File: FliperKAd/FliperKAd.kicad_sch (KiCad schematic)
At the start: 5 parts, among them Q1 NMOS

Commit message: Avancement du PCB
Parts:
- added C10, C9: 100 nF, Capacitor_SMD:C_0402_1005Metric, symbol Device:C_Small
- added C11: 100nF, Capacitor_SMD:C_0603_1608Metric, symbol Device:C_Small
- added C6: 1 µF, Capacitor_SMD:C_0603_1608Metric, symbol Device:C_Small
- added C7: 4.7 µF, Capacitor_SMD:C_0603_1608Metric, symbol Device:C_Small
- added C8: 10 nF, Capacitor_SMD:C_0402_1005Metric, symbol Device:C_Small
- added D2: Green_LED, LED_SMD:LED_0603_1608Metric, symbol Device:LED
- added H1, H2, H3, H4: MountingHole_Pad, MountingHole:MountingHole_3.2mm_M3_Pad_Via, symbol Mechanical:MountingHole_Pad
- added J4: Conn_ST_STDC14, Connector_PinHeader_1.27mm:PinHeader_2x07_P1.27mm_Vertical_SMD, symbol Connector:Conn_ST_STDC14
- added J5: Conn_01x02, Connector_JST:JST_XH_B2B-XH-A_1x02_P2.50mm_Vertical, symbol Connector_Generic:Conn_01x02
- added L2: 39 nH, Inductor_SMD:L_0603_1608Metric, symbol Device:L_Small
- added R2: 1k, Resistor_SMD:R_0603_1608Metric, symbol Device:R_Small
- added U1: STM32G431KBTx, Package_QFP:LQFP-32_7x7mm_P0.8mm, symbol MCU_ST_STM32G4:STM32G431KBTx
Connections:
- net 24V is gone; now on an unnamed net: Q1.3 (S)
- net CommandeBuck: now also U1.9 (PA4)
- net GND: now also C10.2, C11.2, C6.2, C7.2, C8.2, C9.2, H1.1, H2.1, H3.1, H4.1, J4.11 (GNDDetect), J4.5 (GND), J4.7 (GND), J5.2 (Pin_2), R2.2, U1.14 (VSSA), U1.16 (VSS), U1.32 (VSS)
- net at D1.1 (K), L1.1: no longer Q1.1 (D)
- net 3.3V renamed +3.3V
- net +3.3V: now also C10.1, C7.1, C9.1, J4.3 (VCC), L2.2, U1.1 (VDD), U1.17 (VDD)
- new net +24V: J5.1 (Pin_1), Q1.1 (D)
- new net +3.3VA: C6.1, C8.1, L2.1, U1.15 (VDDA)
- new net CommandeSolénoîde: U1.10 (PA5)
- new net LED_Stat: D2.1 (K), R2.1
- new net LED_Status: D2.2 (A), U1.18 (PA8)
- new net NRST: C11.1, J4.12 (~{RST}), U1.4 (PG10)
- new net SYS_SWCLK: J4.6 (JCLK/SWCLK), U1.24 (PA14)
- new net SYS_SWDIO: J4.4 (JTMS/SWDIO), U1.23 (PA13)
- new net USART2_RX: J4.13 (VCP_RX), U1.8 (PA3)
- new net USART2_TX: J4.14 (VCP_TX), U1.7 (PA2)
- no-connect marks 0 -> 15
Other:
- company: (none) -> ENSEA
- title: (none) -> PCB_Solénoide
- moved on the sheet: Q1

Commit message: Fin de séance du 30
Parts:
- added C2: 10 µ, symbol Device:C_Small
- added C3: 1 µ, symbol Device:C_Small
- added C4: 47 µ, symbol Device:C_Small
- added R3: 137k, symbol Device:R_Small
- added R4: 402k, symbol Device:R_Small
- added R5: R_Small, symbol Device:R_Small
- added U2, U3: MCP1640x-xMC, Package_DFN_QFN:DFN-8-1EP_3x2mm_P0.5mm_EP1.75x1.45mm, symbol Lib:MCP1640x-xMC
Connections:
- net +24V: now also C2.1, U2.4 (Vin), U2.5 (Vin)
- net +3.3V: now also C4.1, R4.1, U2.6 (Vout), U2.7 (Vout)
- net GND: now also C2.2, C3.2, C4.2, R3.2, R5.2, U2.10 (AGND), U2.13 (PGND)
- new net: C3.1, U2.1 (FSW)
- new net: R3.1, R4.2, U2.2 (FB)
- new net: R5.1, U2.3 (VCC)
- new net: U2.12 (EN), U2.9 (Vin)
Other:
- note added: "WPME"

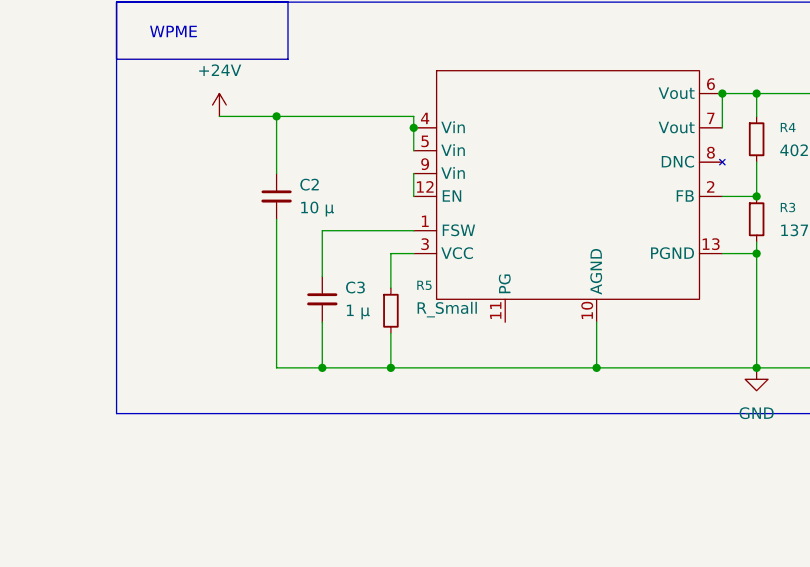
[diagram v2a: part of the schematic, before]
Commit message: Ajout du dossier Doc
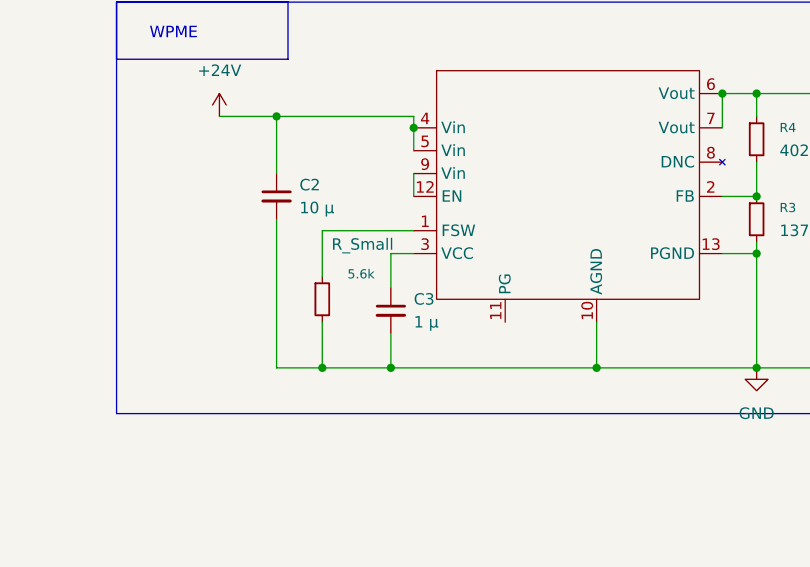
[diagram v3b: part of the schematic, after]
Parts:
- renumbered R5 to 5.6k
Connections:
- net at C3.1: now also U2.3 (VCC); no longer U2.1 (FSW)
- net at 5.6k.1: now also U2.1 (FSW); no longer U2.3 (VCC)
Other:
- moved on the sheet: 5.6k, C3
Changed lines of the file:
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@@
 	)
 	(junction
-		(at 208.28 160.02)
-		(diameter 0)
-		(color 0 0 0 0)
-	)
-	(junction
 		(at 248.92 160.02)
 		(diameter 0)
@@
 	)
 	(junction
-		(at 200.66 160.02)
-		(diameter 0)
-		(color 0 0 0 0)
-	)
-	(junction
 		(at 57.15 173.99)
 		(diameter 0)
@@
 	)
 	(junction
+		(at 208.28 160.02)
+		(diameter 0)
+		(color 0 0 0 0)
+	)
+	(junction
 		(at 243.84 74.93)
 		(diameter 0)
@@
 	)
 	(junction
+		(at 200.66 160.02)
+		(diameter 0)
+		(color 0 0 0 0)
+	)
+	(junction
 		(at 250.19 33.02)
 		(diameter 0)
@@
 	(wire
 		(pts
-			(xy 208.28 147.32) (xy 208.28 151.13)
-		)
-		(stroke
-			(width 0)
-			(type default)
-		)
-	)
-	(wire
-		(pts
 			(xy 243.84 87.63) (xy 261.62 87.63)
 		)
@@
 	(wire
 		(pts
-			(xy 200.66 154.94) (xy 200.66 160.02)
+			(xy 200.66 144.78) (xy 200.66 149.86)
 		)
 		(stroke
@@
 	(wire
 		(pts
-			(xy 200.66 144.78) (xy 200.66 149.86)
+			(xy 200.66 154.94) (xy 200.66 160.02)
 		)
 		(stroke
@@
 	(wire
 		(pts
-			(xy 208.28 156.21) (xy 208.28 160.02)
+			(xy 60.96 88.9) (xy 60.96 91.44)
 		)
 		(stroke
@@
 	(wire
 		(pts
-			(xy 60.96 88.9) (xy 60.96 91.44)
+			(xy 208.28 160.02) (xy 231.14 160.02)
 		)
 		(stroke
@@
 	(wire
 		(pts
+			(xy 208.28 147.32) (xy 208.28 151.13)
+		)
+		(stroke
+			(width 0)
+			(type default)
+		)
+	)
+	(wire
+		(pts
 			(xy 210.82 132.08) (xy 210.82 133.35)
 		)
@@
 	(wire
 		(pts
+			(xy 208.28 156.21) (xy 208.28 160.02)
+		)
+		(stroke
+			(width 0)
+			(type default)
+		)
+	)
+	(wire
+		(pts
 			(xy 261.62 87.63) (xy 261.62 82.55)
 		)
@@
 	(wire
 		(pts
-			(xy 200.66 160.02) (xy 208.28 160.02)
+			(xy 226.06 74.93) (xy 231.14 74.93)
 		)
 		(stroke
@@
 	(wire
 		(pts
-			(xy 226.06 74.93) (xy 231.14 74.93)
+			(xy 200.66 160.02) (xy 208.28 160.02)
 		)
 		(stroke
@@
 	(wire
 		(pts
-			(xy 208.28 160.02) (xy 231.14 160.02)
+			(xy 195.58 160.02) (xy 200.66 160.02)
 		)
 		(stroke
@@
 	(wire
 		(pts
-			(xy 195.58 160.02) (xy 200.66 160.02)
-		)
-		(stroke
-			(width 0)
-			(type default)
-		)
-	)
-	(wire
-		(pts
 			(xy 240.03 60.96) (xy 236.22 60.96)
 		)
@@
 	(symbol
 		(lib_id "Device:C_Small")
-		(at 200.66 152.4 0)
+		(at 208.28 153.67 0)
 		(unit 1)
 		(exclude_from_sim no)
@@
 		(fields_autoplaced yes)
 		(property "Reference" "C3"
-			(at 203.2 151.1362 0)
+			(at 210.82 152.4062 0)
 			(effects
 				(font
@@
 		)
 		(property "Value" "1 µ"
-			(at 203.2 153.6762 0)
+			(at 210.82 154.9462 0)
 			(effects
 				(font
@@
 		)
 		(property "Footprint" ""
-			(at 200.66 152.4 0)
+			(at 208.28 153.67 0)
 			(effects
 				(font
@@
 		)
 		(property "Datasheet" "~"
-			(at 200.66 152.4 0)
+			(at 208.28 153.67 0)
 			(effects
 				(font
@@
 		)
 		(property "Description" "Unpolarized capacitor, small symbol"
-			(at 200.66 152.4 0)
+			(at 208.28 153.67 0)
 			(effects
 				(font
@@
 		(lib_name "R_Small_1")
 		(lib_id "Device:R_Small")
-		(at 208.28 153.67 0)
+		(at 200.66 152.4 0)
 		(unit 1)
 		(exclude_from_sim no)
@@
 		(on_board yes)
 		(dnp no)
-		(property "Reference" "R5"
-			(at 211.074 150.876 0)
+		(property "Reference" "5.6k"
+			(at 203.454 149.606 0)
 			(effects
 				(font
@@
 		)
 		(property "Value" "R_Small"
-			(at 211.074 153.416 0)
+			(at 201.676 146.304 0)
 			(effects
 				(font
@@
 		)
 		(property "Footprint" ""
-			(at 208.28 153.67 0)
+			(at 200.66 152.4 0)
 			(effects
 				(font
@@
 		)
 		(property "Datasheet" "~"
-			(at 208.28 153.67 0)
+			(at 200.66 152.4 0)
 			(effects
 				(font
@@
 		)
 		(property "Description" "Resistor, small symbol"
-			(at 208.28 153.67 0)
+			(at 200.66 152.4 0)
 			(effects
 				(font
@@
 			(project "FliperKAd"
 				(path "/27859523-150b-47ee-b996-34d2328aaeb5"
-					(reference "R5")
+					(reference "5.6k")
 					(unit 1)
 				)

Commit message: Finalisation schematics + empreintes
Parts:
- removed C1: C_Small, symbol Device:C_Small
- removed D1: D_Small, symbol Device:D_Small
- removed D2: Green_LED, LED_SMD:LED_0603_1608Metric, symbol Device:LED
- removed J4: Conn_ST_STDC14, Connector_PinHeader_1.27mm:PinHeader_2x07_P1.27mm_Vertical_SMD, symbol Connector:Conn_ST_STDC14
- removed L1: L_Small, symbol Device:L_Small
- removed Q1: NMOS, symbol Simulation_SPICE:NMOS
- removed R2: 1k, Resistor_SMD:R_0603_1608Metric, symbol Device:R_Small
- removed U2: MCP1640x-xMC, Package_DFN_QFN:DFN-8-1EP_3x2mm_P0.5mm_EP1.75x1.45mm, symbol Lib:MCP1640x-xMC
- added D1: LED_Small, LED_SMD:LED_0603_1608Metric, symbol Device:LED_Small
- added J1: Conn_01x02, Connector_JST:JST_XH_B2B-XH-A_1x02_P2.50mm_Vertical, symbol Connector_Generic:Conn_01x02
- added J2: Conn_ST_STDC14, Connector_PinHeader_1.27mm:PinHeader_2x07_P1.27mm_Vertical_SMD, symbol Connector:Conn_ST_STDC14
- added TP1: 24V, TestPoint:TestPoint_Pad_D2.0mm, symbol Connector:TestPoint
- added TP2: 3.3V, TestPoint:TestPoint_Pad_D2.0mm, symbol Connector:TestPoint
- C2, C3, C4: footprint (none) -> Capacitor_SMD:C_0603_1608Metric
- R1: value R_Small -> 1k; footprint (none) -> Resistor_SMD:R_0603_1608Metric
- R3, R4: footprint (none) -> Resistor_SMD:R_0603_1608Metric
- R5: renamed from 5.6k; value R_Small -> 5.6k; footprint (none) -> Resistor_SMD:R_0603_1608Metric
- U3: footprint Package_DFN_QFN:DFN-8-1EP_3x2mm_P0.5mm_EP1.75x1.45mm -> Perso:WPME_Magic
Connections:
- net +24V: now also U3.4 (Vin), U3.5 (Vin), TP1.1
- net +3.3V: now also U3.6 (Vout), U3.7 (Vout), J2.3 (VCC), TP2.1; no longer R1.1
- net GND: now also U3.10 (AGND), U3.13 (PGND), J1.2 (Pin_2), J2.11 (GNDDetect), J2.5 (GND), J2.7 (GND)
- net LED_Stat: now also R1.1, D1.1 (K)
- net LED_Status: now also D1.2 (A)
- net NRST: now also J2.12 (~{RST})
- net SYS_SWCLK: now also J2.6 (JCLK/SWCLK)
- net SYS_SWDIO: now also J2.4 (JTMS/SWDIO)
- net USART2_RX: now also J2.13 (VCP_RX)
- net USART2_TX: now also J2.14 (VCP_TX)
- net at C3.1: now also U3.3 (VCC)
- net at R3.1, R4.2: now also U3.2 (FB)
- net Bouton_Actif: now reaches U1.19 (PA9)
- net Bouton_Actif: now also J1.1 (Pin_1)
- net at U3.1 (FSW): now also R5.1
- net at U3.12 (EN): now also U3.9 (Vin)
- net CommandeBuck: no longer names the net of U1.9 (PA4)
- net CommandeSolénoîde: no longer names the net of U1.10 (PA5)
- no-connect marks 15 -> 23
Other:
- note added: "Programmer"
- note removed: "Buck"
- moved on the sheet: J5

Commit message: PCB Routé
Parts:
- added JP1: SolderJumper_2_Open, Jumper:SolderJumper-2_P1.3mm_Open_TrianglePad1.0x1.5mm, symbol Jumper:SolderJumper_2_Open
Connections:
- net +3.3V: now also JP1.2 (B); no longer C4.1, R4.1, TP2.1, U3.6 (Vout), U3.7 (Vout)
- new net Test 3.3: C4.1, JP1.1 (A), R4.1, TP2.1, U3.6 (Vout), U3.7 (Vout)
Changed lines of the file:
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@@
 	(wire
 		(pts
-			(xy 269.24 129.54) (xy 274.32 129.54)
+			(xy 269.24 129.54) (xy 273.05 129.54)
 		)
 		(stroke
@@
 	(wire
 		(pts
-			(xy 95.25 66.04) (xy 73.66 66.04)
+			(xy 77.47 66.04) (xy 73.66 66.04)
 		)
 		(stroke
@@
 	(wire
 		(pts
+			(xy 78.74 63.5) (xy 73.66 63.5)
+		)
+		(stroke
+			(width 0)
+			(type default)
+		)
+	)
+	(wire
+		(pts
 			(xy 60.96 88.9) (xy 60.96 91.44)
 		)
@@
 	(wire
 		(pts
+			(xy 280.67 127) (xy 280.67 129.54)
+		)
+		(stroke
+			(width 0)
+			(type default)
+		)
+	)
+	(wire
+		(pts
 			(xy 195.58 132.08) (xy 203.2 132.08)
 		)
@@
 		)
 	)
+	(label "Test 3.3"
+		(at 252.73 129.54 0)
+		(effects
+			(font
+				(size 1.27 1.27)
+			)
+			(justify left bottom)
+		)
+	)
 	(label "LED_Stat"
 		(at 21.59 100.33 0)
@@
 	(global_label "Bouton_Actif"
 		(shape input)
-		(at 95.25 66.04 0)
+		(at 77.47 66.04 0)
 		(fields_autoplaced yes)
 		(effects
@@
 		)
 		(property "Intersheetrefs" "${INTERSHEET_REFS}"
-			(at 110.0279 66.04 0)
+			(at 92.2479 66.04 0)
 			(effects
 				(font
@@
 	(global_label "LED_Status"
 		(shape input)
-		(at 73.66 63.5 0)
+		(at 78.74 63.5 0)
 		(fields_autoplaced yes)
 		(effects
@@
 		)
 		(property "Intersheetrefs" "${INTERSHEET_REFS}"
-			(at 87.0469 63.5 0)
+			(at 92.1269 63.5 0)
 			(effects
 				(font
@@
 	)
 	(symbol
+		(lib_id "Jumper:SolderJumper_2_Open")
+		(at 276.86 129.54 0)
+		(unit 1)
+		(exclude_from_sim no)
+		(in_bom no)
+		(on_board yes)
+		(dnp no)
+		(fields_autoplaced yes)
+		(property "Reference" "JP1"
+			(at 276.86 123.19 0)
+			(effects
+				(font
+					(size 1.27 1.27)
+				)
+			)
+		)
+		(property "Value" "SolderJumper_2_Open"
+			(at 276.86 125.73 0)
+			(effects
+				(font
+					(size 1.27 1.27)
+				)
+			)
+		)
+		(property "Footprint" "Jumper:SolderJumper-2_P1.3mm_Open_TrianglePad1.0x1.5mm"
+			(at 276.86 129.54 0)
+			(effects
+				(font
+					(size 1.27 1.27)
+				)
+				(hide yes)
+			)
+		)
+		(property "Datasheet" "~"
+			(at 276.86 129.54 0)
+			(effects
+				(font
+					(size 1.27 1.27)
+				)
+				(hide yes)
+			)
+		)
+		(property "Description" "Solder Jumper, 2-pole, open"
+			(at 276.86 129.54 0)
+			(effects
+				(font
+					(size 1.27 1.27)
+				)
+				(hide yes)
+			)
+		)
+		(pin "2"
+		)
+		(pin "1"
+		)
+		(instances
+			(project ""
+				(path "/27859523-150b-47ee-b996-34d2328aaeb5"
+					(reference "JP1")
+					(unit 1)
+				)
+			)
+		)
+	)
+	(symbol
 		(lib_id "Mechanical:MountingHole_Pad")
 		(at 259.08 20.32 270)
@@
 	(symbol
 		(lib_id "power:+3.3V")
-		(at 274.32 129.54 0)
+		(at 280.67 127 0)
 		(unit 1)
 		(exclude_from_sim no)
@@
 		(fields_autoplaced yes)
 		(property "Reference" "#PWR017"
-			(at 274.32 133.35 0)
+			(at 280.67 130.81 0)
 			(effects
 				(font
@@
 		)
 		(property "Value" "+3.3V"
-			(at 274.32 124.46 0)
+			(at 280.67 121.92 0)
 			(effects
 				(font
@@
 		)
 		(property "Footprint" ""
-			(at 274.32 129.54 0)
+			(at 280.67 127 0)
 			(effects
 				(font
@@
 		)
 		(property "Datasheet" ""
-			(at 274.32 129.54 0)
+			(at 280.67 127 0)
 			(effects
 				(font
@@
 		)
 		(property "Description" "Power symbol creates a global label with name \"+3.3V\""
-			(at 274.32 129.54 0)
+			(at 280.67 127 0)
 			(effects
 				(font

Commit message: Manque un truc
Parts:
- added J3: Conn_01x02, Connector_JST:JST_XH_B2B-XH-A_1x02_P2.50mm_Vertical, symbol Connector_Generic:Conn_01x02
- added Q1: NMOS, symbol Simulation_SPICE:NMOS
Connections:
- net GND: now also J3.2 (Pin_2)
- net Com-Sol: now reaches U1.20 (PA10)
- net Com-Sol: now also Q1.2 (G)
- new net Sortie-Solénoide: J3.1 (Pin_1)
- no-connect marks 23 -> 22

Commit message: just in time
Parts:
- added D2, D3: 1N4148WS, Diode_SMD:D_SOD-323, symbol Diode:1N4148WS
- added J4: Conn_01x02, Connector_JST:JST_XH_B2B-XH-A_1x02_P2.50mm_Vertical, symbol Connector_Generic:Conn_01x02
- added Q2: NMOS, Package_TO_SOT_SMD:TO-263-3_TabPin4, symbol Simulation_SPICE:NMOS
- added R10, R11: 4.7, Resistor_SMD:R_0603_1608Metric, symbol Device:R_Small
- added R12, R2, R6, R7, R8, R9: 10k, Resistor_SMD:R_0603_1608Metric, symbol Device:R_Small
- added U4: ~, Perso:MIC4426, symbol Lib:MIC4426
- Q1: footprint (none) -> Package_TO_SOT_SMD:TO-263-3_TabPin4
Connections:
- net Sortie-Solénoide is gone; now on net +24V: J3.1 (Pin_1)
- net +24V: now also D2.1 (K), D3.1 (K), J4.1 (Pin_1), R6.1
- net GND: now also Q1.3 (S), Q2.3 (S), R12.2, R2.2, R7.2, R8.2, R9.2, U4.3 (GND); no longer J3.2 (Pin_2)
- net Sortie-SolénoideA: now reaches Q1.1 (D)
- net Sortie-SolénoideA: now also J3.2 (Pin_2), D2.2 (A)
- net Com-SolB: now reaches U1.21 (PA11)
- net Com-SolB: now also R7.1, U4.4 (INB)
- net Com-Sol: no longer names the net of Q1.2 (G)
- net Com-Sol: now also R10.1, R9.1; no longer U1.20 (PA10)
- new net: Q2.2 (G), R11.1, R12.1
- new net +12V: R2.1, R6.2, U4.6 (Vs)
- new net Com-MOSA: R10.2, U4.7 (OUTA)
- new net Com-MOSB: R11.2, U4.5 (OUTB)
- new net Com-SolA: R8.1, U1.20 (PA10), U4.2 (INA)
- new net Sortie-SolénoideB: D3.2 (A), J4.2 (Pin_2), Q2.1 (D)
- no-connect marks 22 -> 21
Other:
- note added: "DRIVER des MOS"
- note added: "MOSFETA"
- note added: "MOSFETB"
- moved on the sheet: Q1

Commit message: pcb fini plus routage à valider et commander
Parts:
- removed R2, R6: 10k, Resistor_SMD:R_0603_1608Metric, symbol Device:R_Small
- added C1: 100nF, Capacitor_SMD:C_0603_1608Metric, symbol Device:C_Small
- added C12, C5: 10 µ, Capacitor_SMD:C_0603_1608Metric, symbol Device:C_Small
- added JP2: SolderJumper_2_Open, Jumper:SolderJumper-2_P1.3mm_Open_TrianglePad1.0x1.5mm, symbol Jumper:SolderJumper_2_Open
- added TP3: 12V, TestPoint:TestPoint_Pad_D2.0mm, symbol Connector:TestPoint
- added U5: ~, Perso:173951275, symbol Lib:173951275_
- D2, D3: value 1N4148WS -> FSV340AF; footprint Diode_SMD:D_SOD-323 -> Diode_SMD:D_SMA
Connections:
- net +12V: now also C1.1, JP2.2 (B), TP3.1
- net +24V: now also U3.12 (EN), U3.9 (Vin), C5.1, U5.1 (Vin)
- net GND: now also C1.2, C12.2, U5.2 (Gnd)
- new net: C12.1, C5.2
- new net 12test: JP2.1 (A), U5.3 (Vout)
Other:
- note added: "WPME 12V"
- note added: "WPME 3.3V"
- note removed: "WPME"
- moved on the sheet: J2
